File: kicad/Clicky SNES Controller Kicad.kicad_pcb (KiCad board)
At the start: 2 copper layers, 41.9 x 44.8 mm, 39 parts, among them CN1 CN1, P11 TL_IN, P13 TR_IN, P2 VSS_Trigger, P3 TR_TL_OUT, P4 DPAD_IN, P6 ABXY_IN, U1 4021, U2 4021, X1 SW_PUSH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

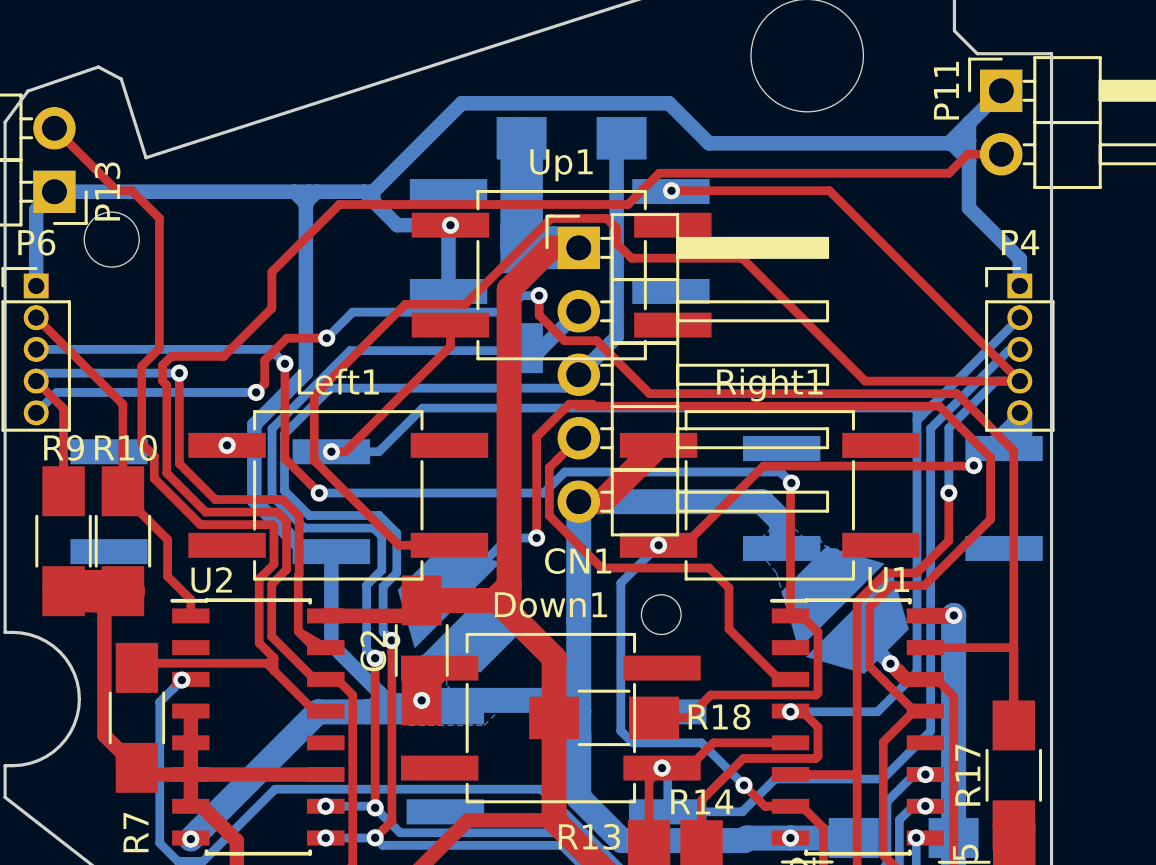
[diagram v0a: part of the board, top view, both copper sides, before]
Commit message: PCB: Fix some DRC errors
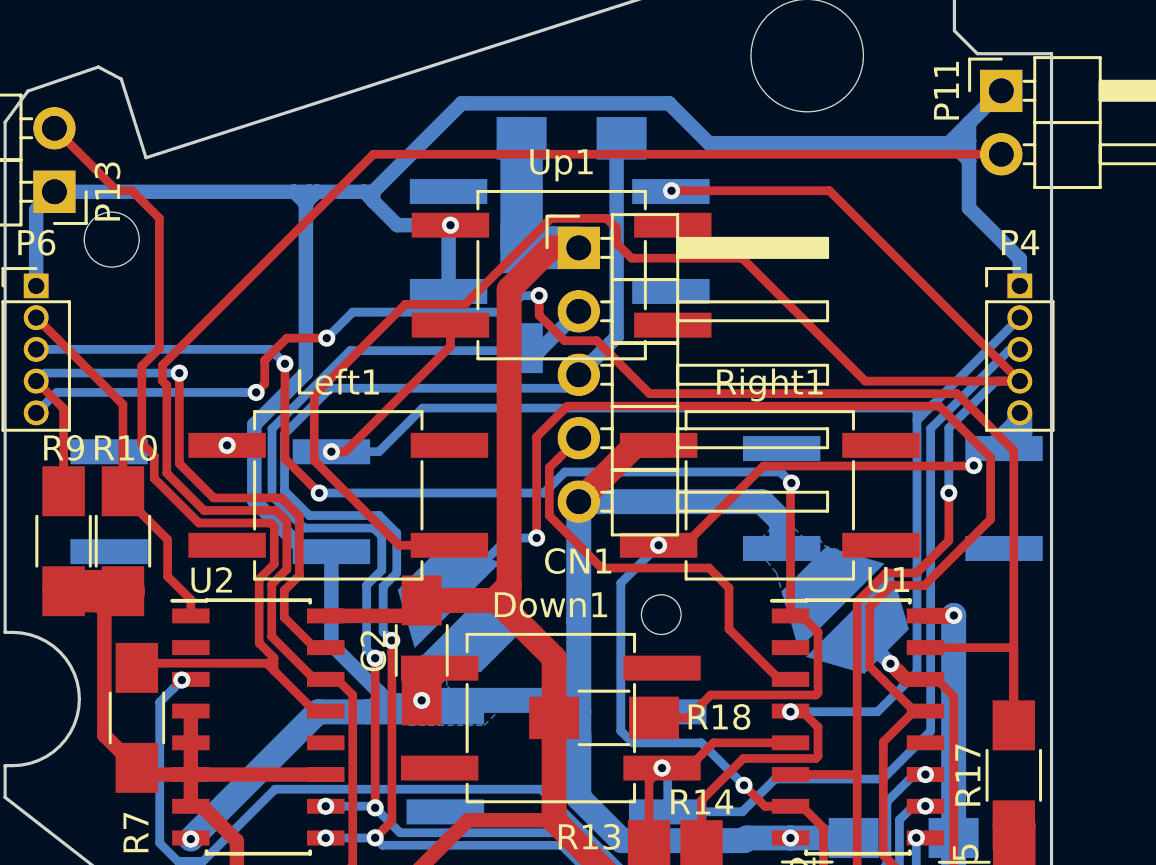
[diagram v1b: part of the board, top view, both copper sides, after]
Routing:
- net /X: track 28.3 -> 26.6 mm
- net /TL: track 67.5 -> 66.7 mm
- net /Start: track 51.0 -> 50.3 mm

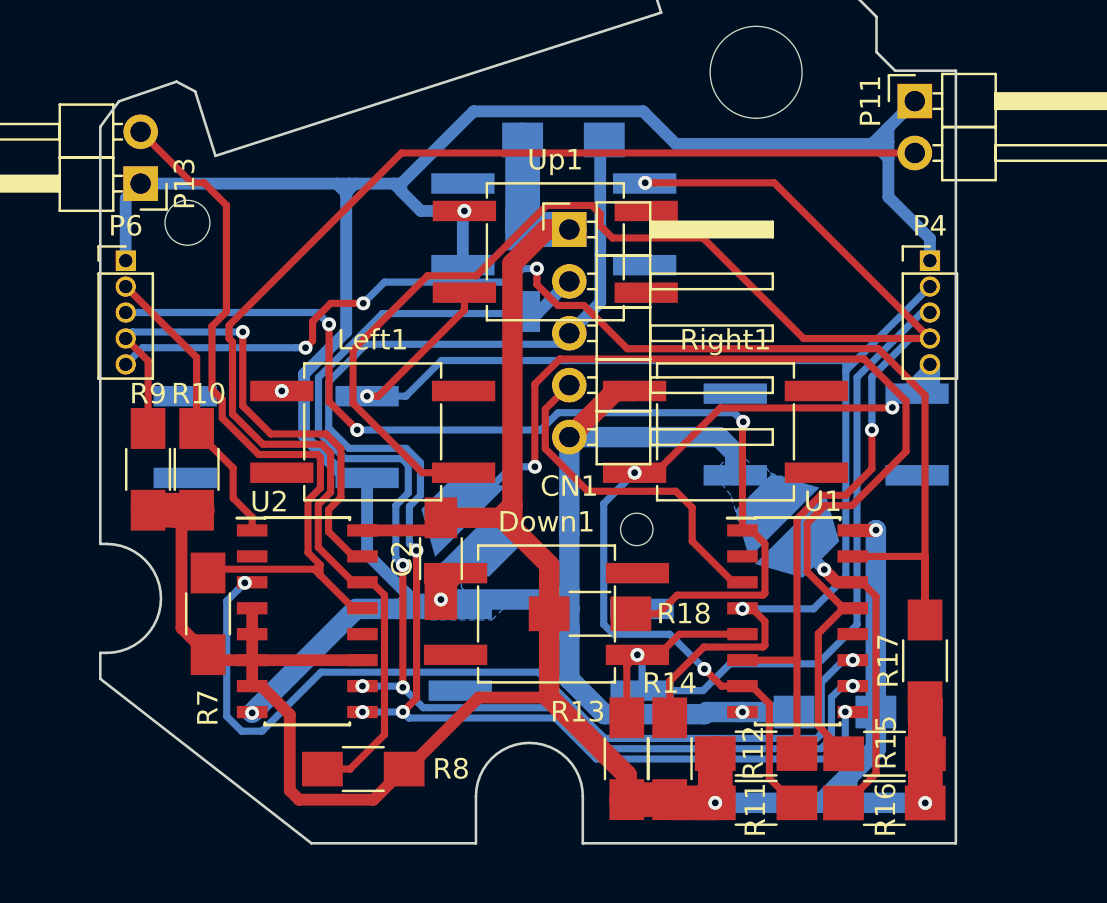
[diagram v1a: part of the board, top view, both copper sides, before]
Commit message: change pads on passives to non hand-soldering versions
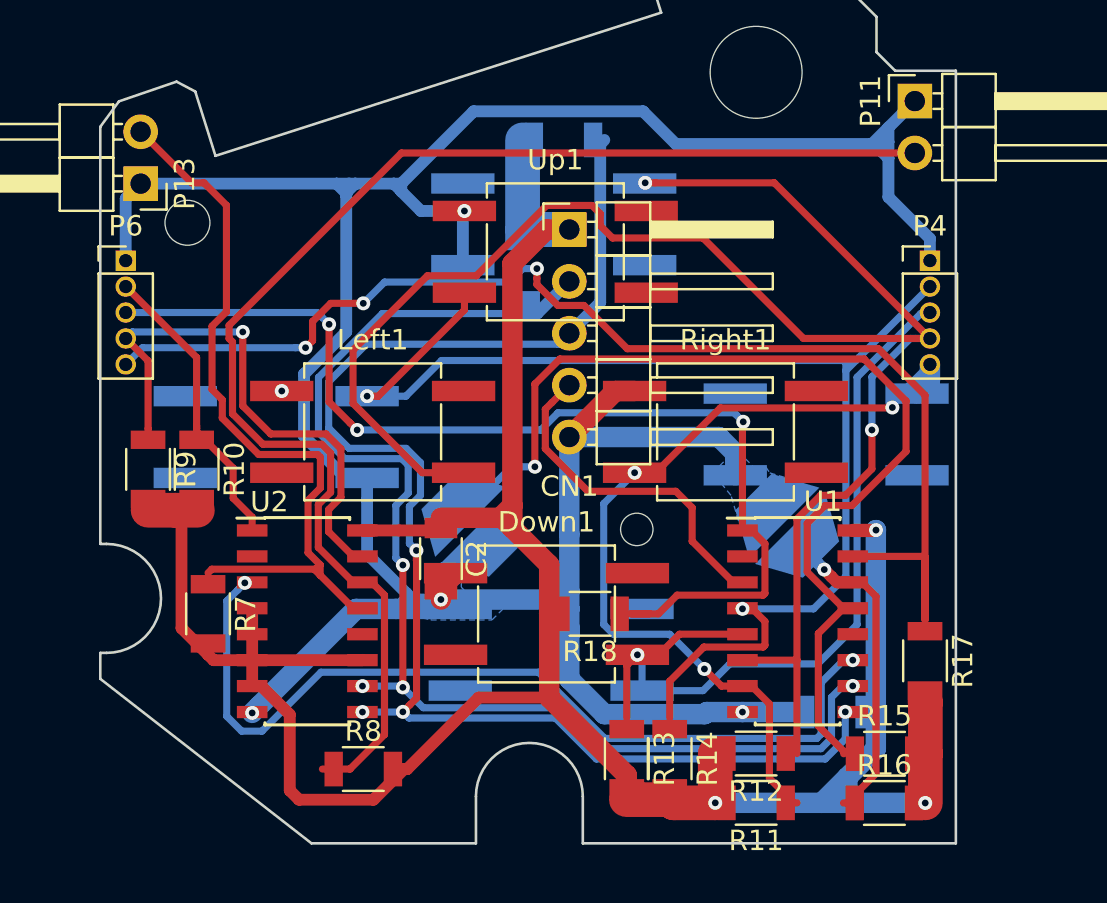
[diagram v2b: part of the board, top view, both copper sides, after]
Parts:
- C1, C2: footprint Capacitors_SMD:C_1206_HandSoldering -> Capacitors_SMD:C_1206
- R1, R10, R11, R12, R13, R14, R15, R16, R17, R18, R2, R7, R8, R9: footprint Resistors_SMD:R_1206_HandSoldering -> Resistors_SMD:R_1206

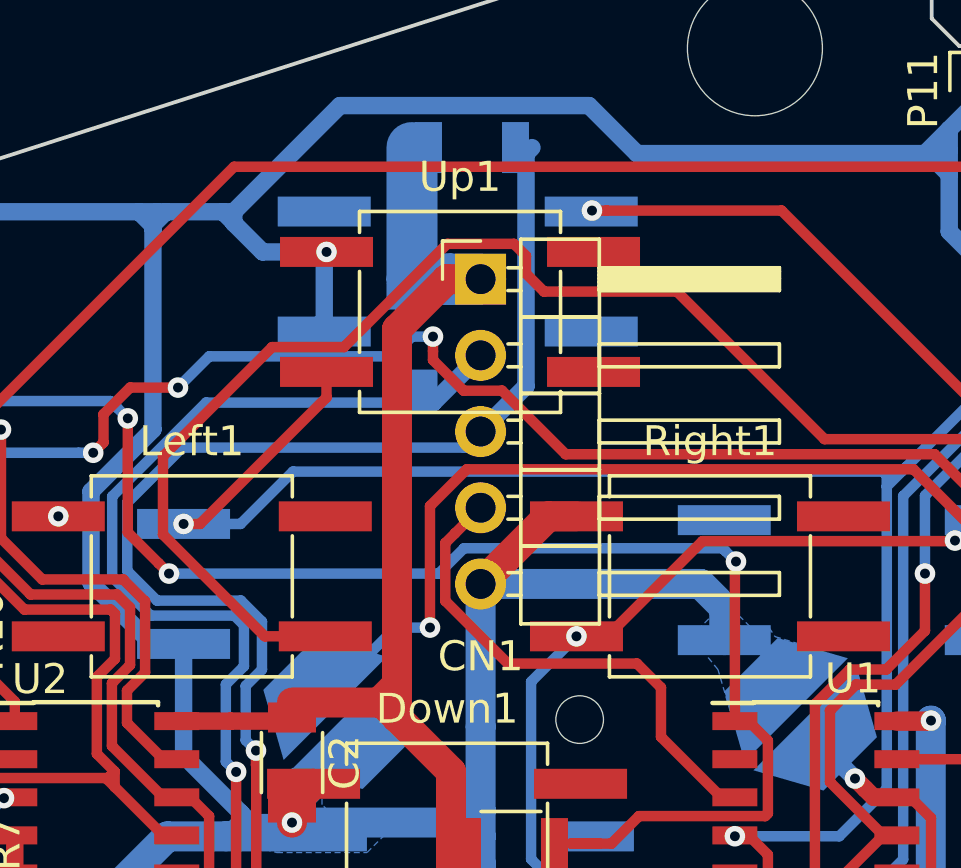
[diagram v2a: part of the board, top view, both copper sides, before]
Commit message: Rotate CN1 180° to fix silkscreen marking
Instead of rotating this and having to renumber all of the pins
I created a new footprint that was mirror-imaged to be left-facing.
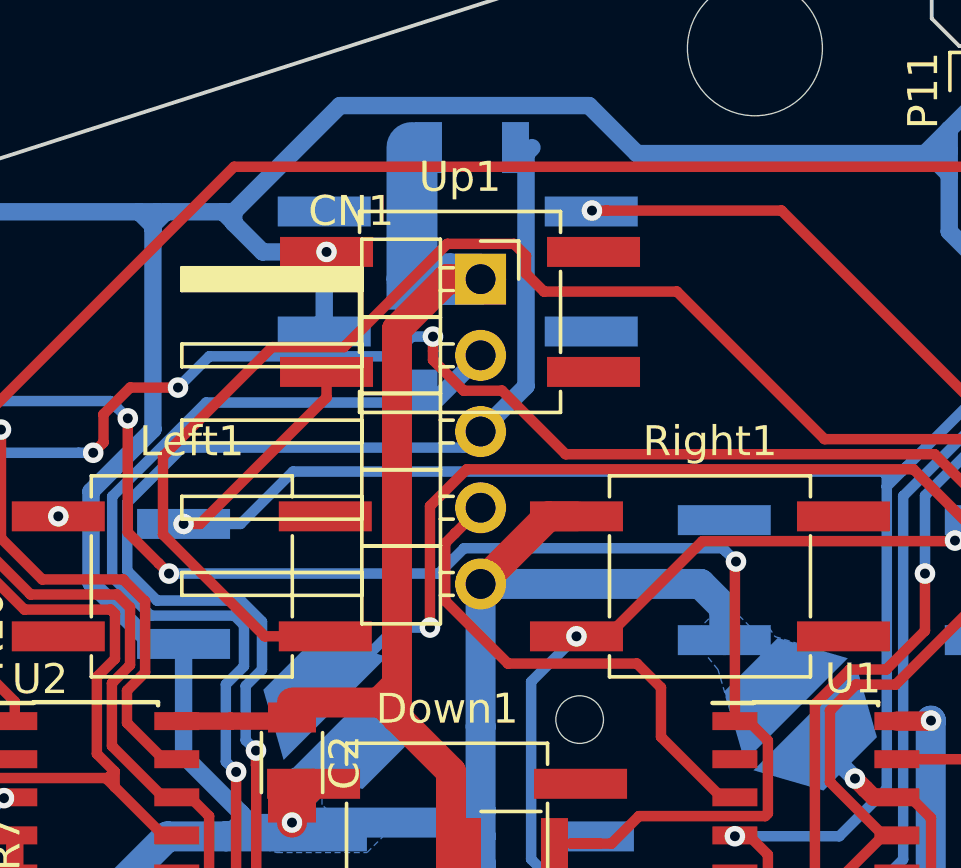
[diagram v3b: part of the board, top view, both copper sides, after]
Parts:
- CN1: footprint Pin_Headers:Pin_Header_Angled_1x05_Pitch2.54mm -> Extra_Pin_Headers:Pin_Header_Angled_1x05_Pitch2.54mm_Sinister

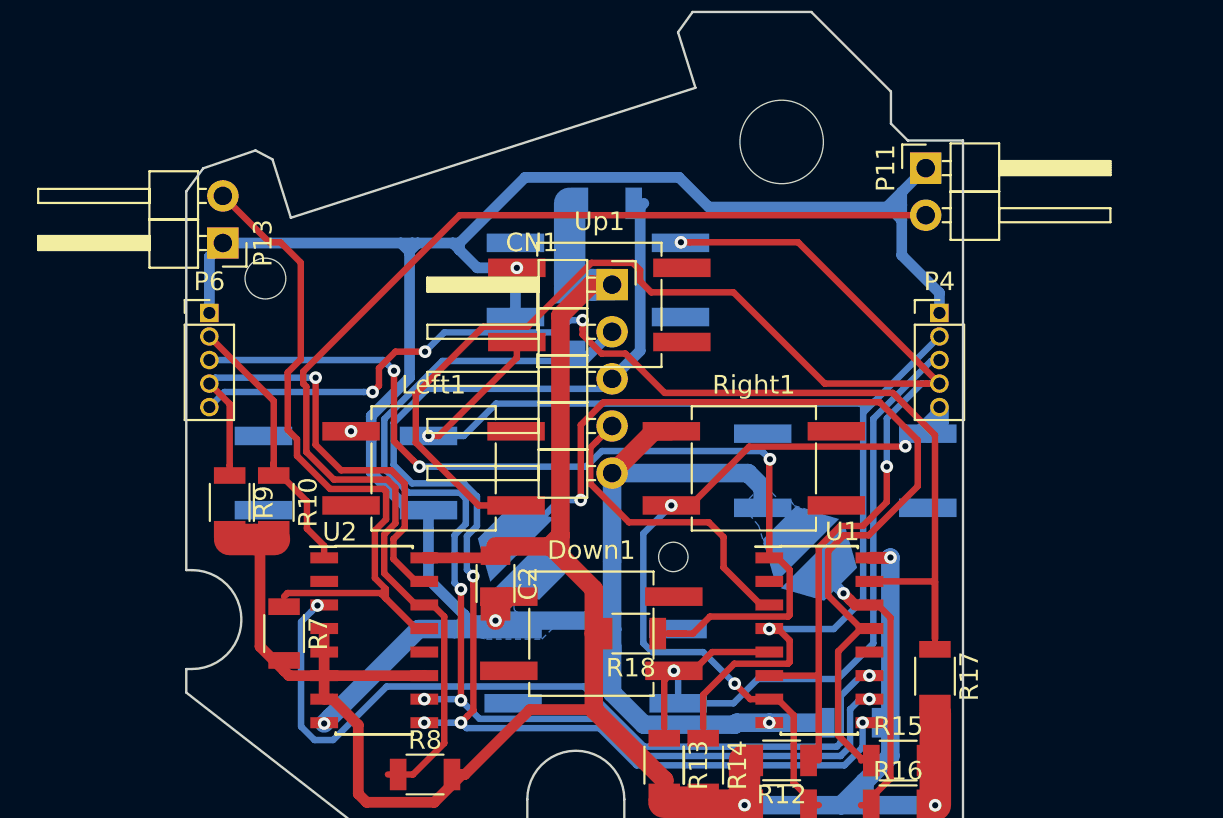
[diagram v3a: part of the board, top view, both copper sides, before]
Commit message: Route TR/TL through the board-to-board connectors
Having TR and TL connectors on the main board puts them too far
away from the trigger boards. This prevents the existing wires
on those boards from being reused.

Move the connectors to the center of the top edge of the ABXY
and DPAD boards (a single connector can be used on both boards).
This combines P11 and P13 (now P15).

P15 is routed straight to the board-to-board connectors so that
it can be brought onto the main board. This changes these from
1x5 to 1x6 pin headers. I have changed the designator for these:
P4 -> P14
P6 -> P16

I have also changed the board-to-board connectors to 2.54mm
pitch because the 1.27mm pitch was extremely tedious to hand-
solder.
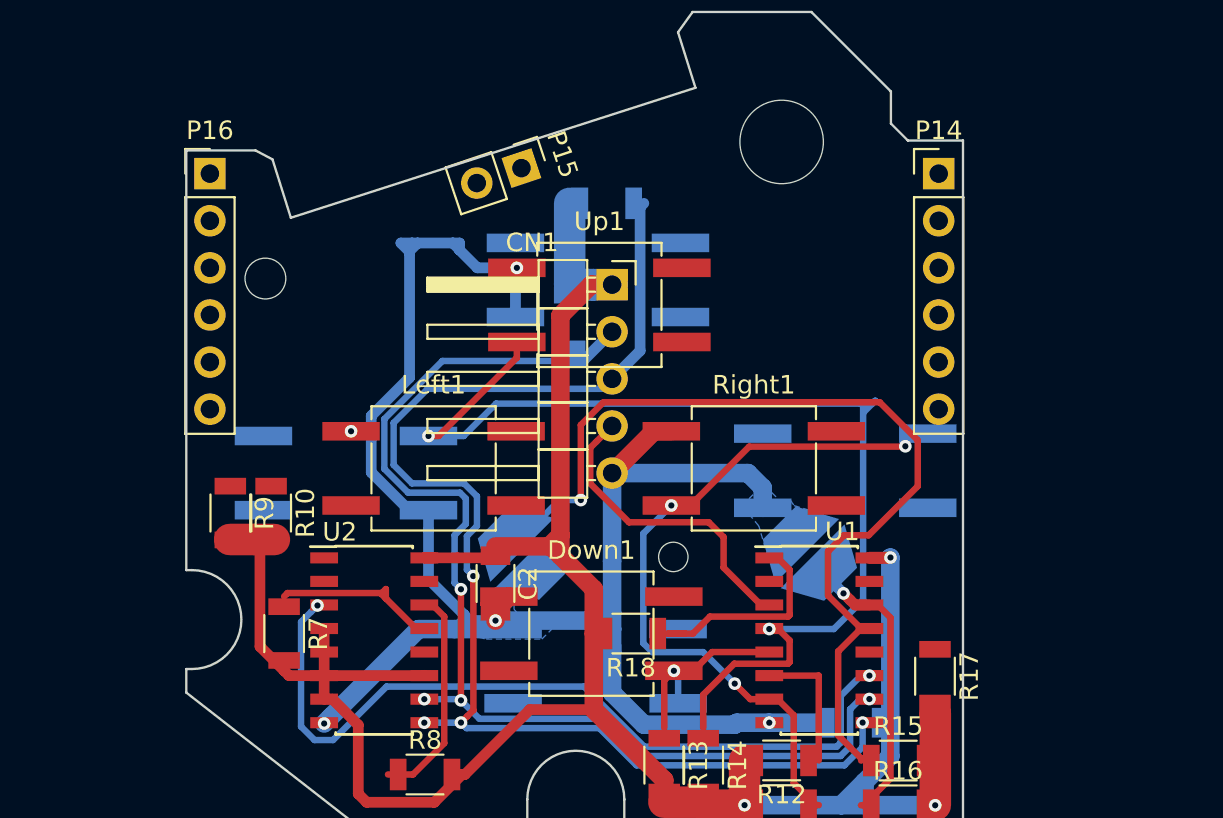
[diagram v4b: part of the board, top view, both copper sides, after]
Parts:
- removed P11: TL_IN, Pin_Headers:Pin_Header_Angled_1x02_Pitch2.54mm
- removed P13: TR_IN, Pin_Headers:Pin_Header_Angled_1x02_Pitch2.54mm
- removed P4: DPAD_IN, Pin_Headers:Pin_Header_Straight_1x05_Pitch1.27mm
- removed P6: ABXY_IN, Pin_Headers:Pin_Header_Straight_1x05_Pitch1.27mm
- added P14: DPAD_IN, Pin_Headers:Pin_Header_Straight_1x06_Pitch2.54mm, F.Cu at (53.3, 21.7)
- added P15: TR_TL_IN, Pin_Headers:Pin_Header_Straight_1x02_Pitch2.54mm, F.Cu at (30.8, 21.4)
- added P16: ABXY_IN, Pin_Headers:Pin_Header_Straight_1x06_Pitch2.54mm, F.Cu at (14.0, 21.7)
- moved R10 0.59 mm to (17.3, 40.0)
- moved R9 0.57 mm to (15.1, 40.0)
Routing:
- net /Left: track 87.7 -> 7.24 mm, vias 2 -> 0
- net /Y: track 62.3 -> 0.00 mm, vias 3 -> 0
- net /TL: track 66.7 -> 12.4 mm
- net GND: track 160.9 -> 109.5 mm
- net /B: track 52.4 -> 11.7 mm, vias 3 -> 0
- net /B_switch: track 39.6 -> 10.7 mm
- net /TR: track 37.7 -> 9.75 mm
- net /X: track 26.6 -> 0.45 mm, vias 1 -> 0
- net /A: track 14.7 -> 0.00 mm
- net /A_switch: track 65.0 -> 60.1 mm
- net /Right: track 41.8 -> 37.5 mm
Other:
- outline, holes or cut-outs redrawn
